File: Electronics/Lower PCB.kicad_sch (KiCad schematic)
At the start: 30 parts, among them J6 Conn_01x04_Male, SW1 Left, SW2 Right, U1 QRE1113GR, U13 TCST2103, TCST2202, TCST2300, U14 TCST2103, TCST2202, TCST2300, U2 QRE1113GR, U3 QRE1113GR, U4 QRE1113GR, U5 QRE1113GR

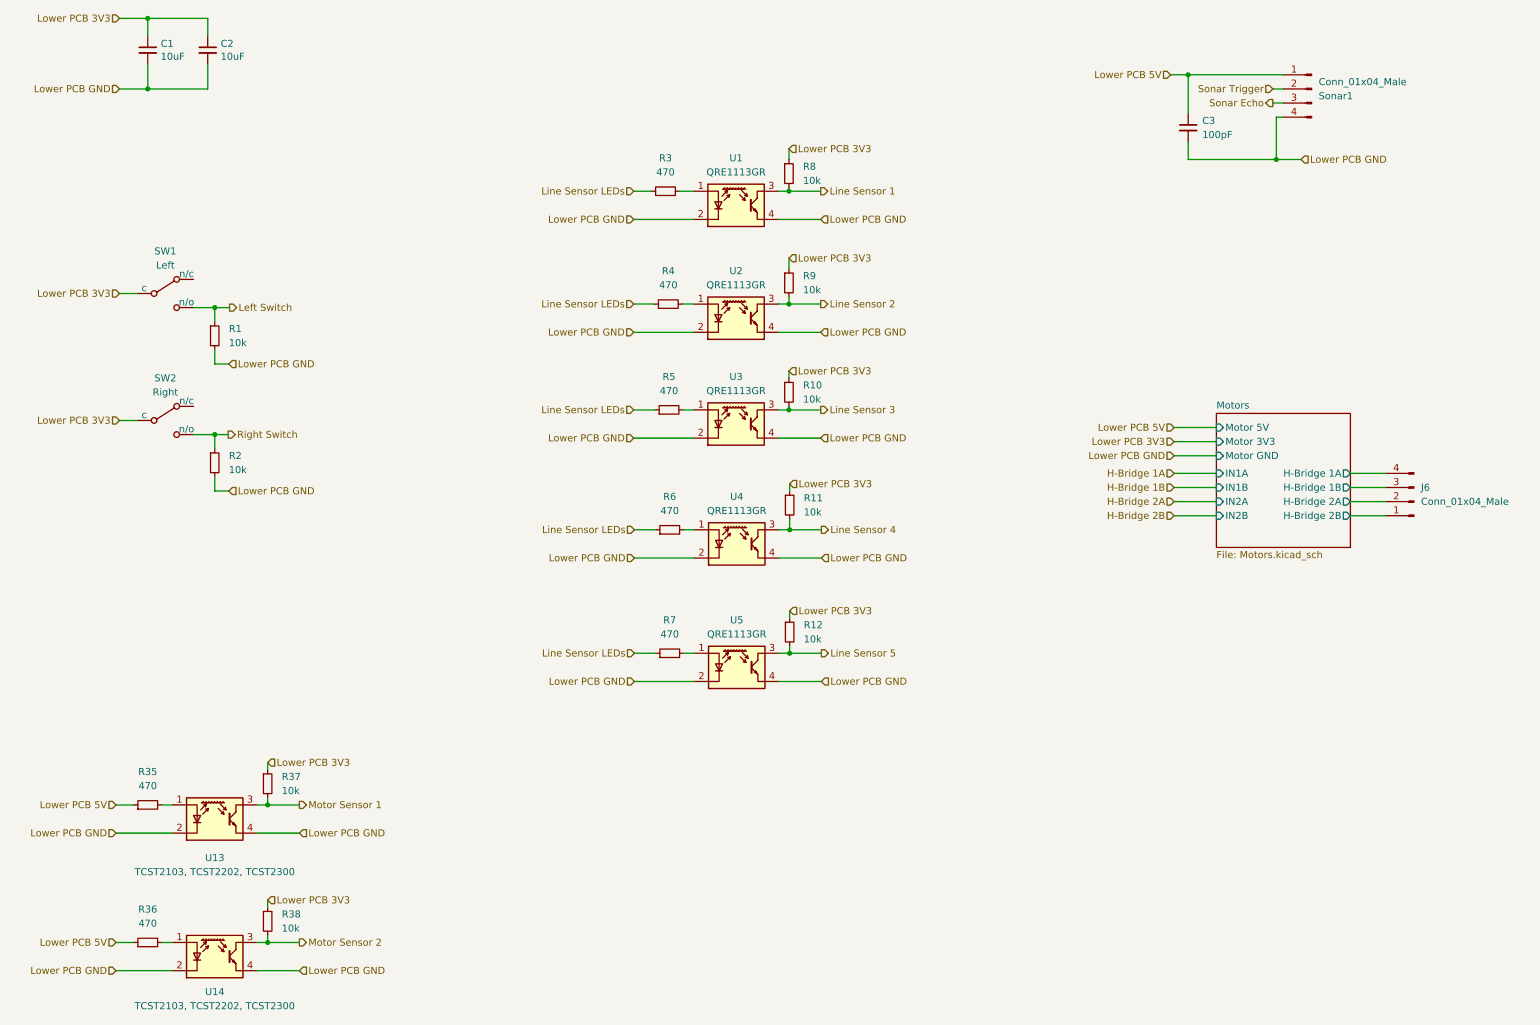
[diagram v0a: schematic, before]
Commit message: added bom
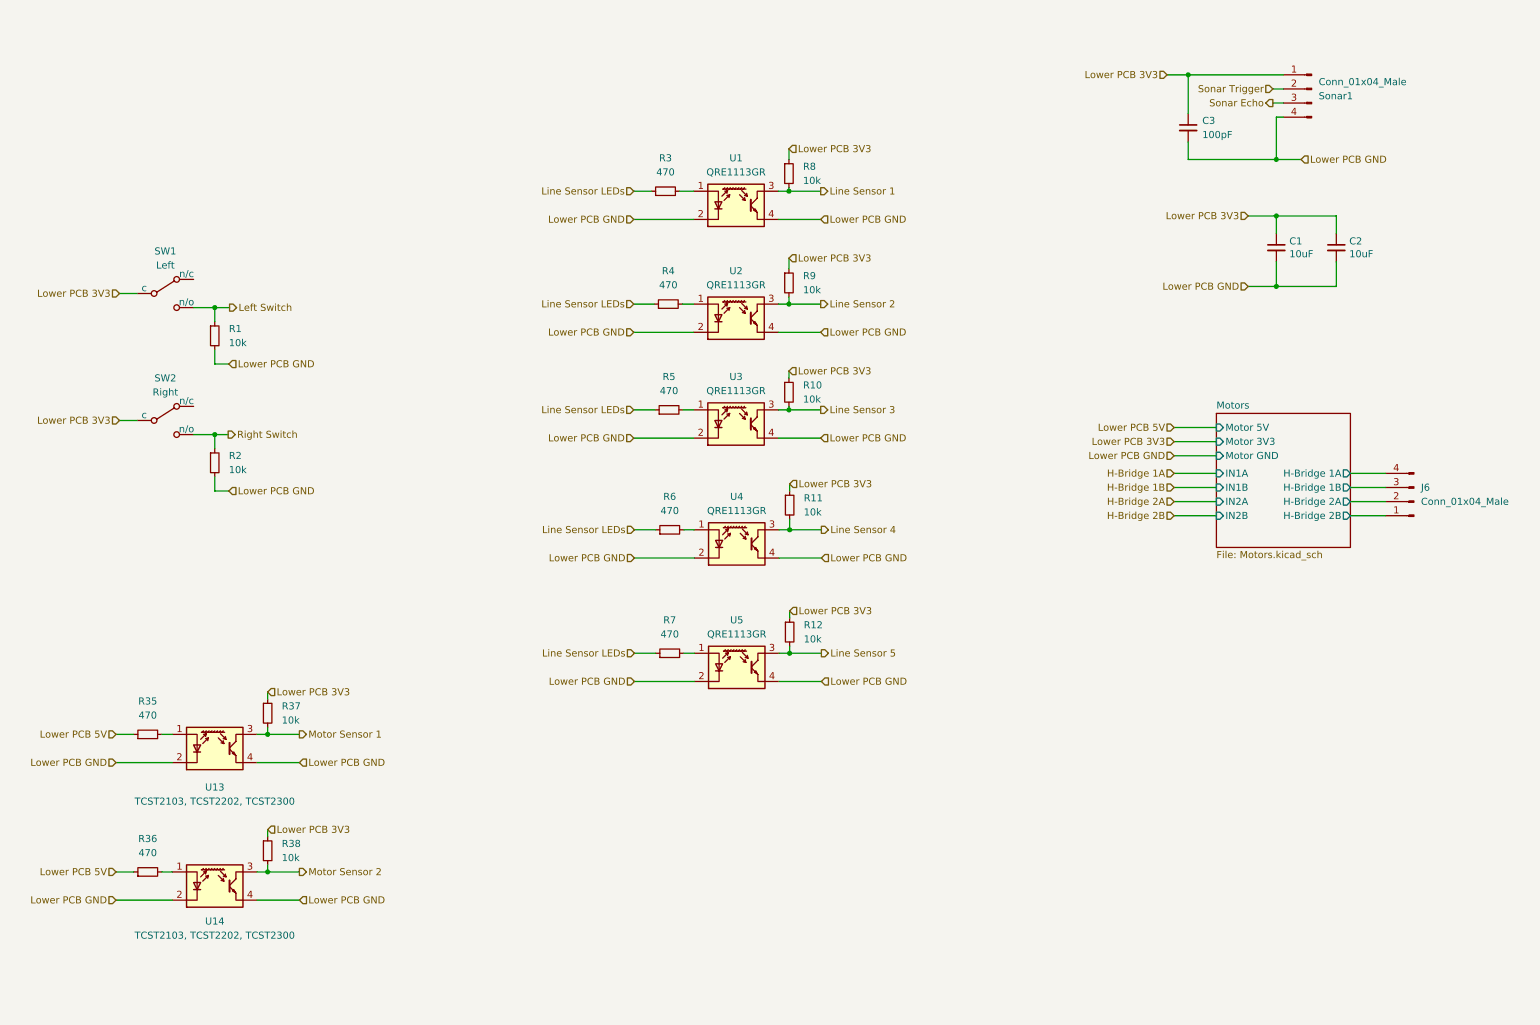
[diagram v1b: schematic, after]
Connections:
- net Lower PCB 3V3: now also C3.1, Sonar1.1 (Pin_1)
- net Lower PCB 5V: no longer C3.1, Sonar1.1 (Pin_1)
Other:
- moved on the sheet: C1, C2, R35, R36, R37, R38, U13, U14

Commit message: del backups
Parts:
- renumbered C3 to C7, C1 to C8, C2 to C9, J6 to J4, R35 to R1, R6 to R10, R7 to R11, R8 to R12, R9 to R13, R10 to R14, R11 to R15, R12 to R16, R36 to R2, R1 to R3, R2 to R4, R37 to R5, R38 to R6, R3 to R7, R4 to R8, R5 to R9, U13 to U2, U14 to U3, U1 to U4, U2 to U5, U3 to U6, U4 to U7, U5 to U8
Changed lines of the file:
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@@
   (symbol (lib_id "Device:R_Small") (at 43.815 149.225 90) (unit 1)
     (in_bom yes) (on_board yes) (fields_autoplaced)
-    (property "Reference" "R35" (id 0) (at 43.815 143.256 90))
+    (property "Reference" "R1" (id 0) (at 43.815 143.256 90))
     (property "Value" "470" (id 1) (at 43.815 145.796 90))
     (property "Footprint" "Resistor_SMD:R_0805_2012Metric_Pad1.20x1.40mm_HandSolder" (id 2) (at 43.815 149.225 0)
@@
   (symbol (lib_id "Device:R_Small") (at 43.815 173.99 90) (unit 1)
     (in_bom yes) (on_board yes) (fields_autoplaced)
-    (property "Reference" "R36" (id 0) (at 43.815 168.021 90))
+    (property "Reference" "R2" (id 0) (at 43.815 168.021 90))
     (property "Value" "470" (id 1) (at 43.815 170.561 90))
     (property "Footprint" "Resistor_SMD:R_0805_2012Metric_Pad1.20x1.40mm_HandSolder" (id 2) (at 43.815 173.99 0)
@@
   (symbol (lib_id "Device:R_Small") (at 55.88 77.47 0) (unit 1)
     (in_bom yes) (on_board yes) (fields_autoplaced)
-    (property "Reference" "R1" (id 0) (at 58.42 76.1999 0)
+    (property "Reference" "R3" (id 0) (at 58.42 76.1999 0)
       (effects (font (size 1.27 1.27)) (justify left))
     )
@@
   (symbol (lib_id "Device:R_Small") (at 55.88 100.33 0) (unit 1)
     (in_bom yes) (on_board yes) (fields_autoplaced)
-    (property "Reference" "R2" (id 0) (at 58.42 99.0599 0)
+    (property "Reference" "R4" (id 0) (at 58.42 99.0599 0)
       (effects (font (size 1.27 1.27)) (justify left))
     )
@@
   (symbol (lib_id "Device:R_Small") (at 65.405 145.415 0) (unit 1)
     (in_bom yes) (on_board yes) (fields_autoplaced)
-    (property "Reference" "R37" (id 0) (at 67.945 144.1449 0)
+    (property "Reference" "R5" (id 0) (at 67.945 144.1449 0)
       (effects (font (size 1.27 1.27)) (justify left))
     )
@@
   (symbol (lib_id "Device:R_Small") (at 65.405 170.18 0) (unit 1)
     (in_bom yes) (on_board yes) (fields_autoplaced)
-    (property "Reference" "R38" (id 0) (at 67.945 168.9099 0)
+    (property "Reference" "R6" (id 0) (at 67.945 168.9099 0)
       (effects (font (size 1.27 1.27)) (justify left))
     )
@@
   (symbol (lib_id "Device:R_Small") (at 137.033 51.435 90) (unit 1)
     (in_bom yes) (on_board yes) (fields_autoplaced)
-    (property "Reference" "R3" (id 0) (at 137.033 45.466 90))
+    (property "Reference" "R7" (id 0) (at 137.033 45.466 90))
     (property "Value" "470" (id 1) (at 137.033 48.006 90))
     (property "Footprint" "Resistor_SMD:R_0805_2012Metric_Pad1.20x1.40mm_HandSolder" (id 2) (at 137.033 51.435 0)
@@
   (symbol (lib_id "Device:R_Small") (at 137.541 71.755 90) (unit 1)
     (in_bom yes) (on_board yes) (fields_autoplaced)
-    (property "Reference" "R4" (id 0) (at 137.541 65.786 90))
+    (property "Reference" "R8" (id 0) (at 137.541 65.786 90))
     (property "Value" "470" (id 1) (at 137.541 68.326 90))
     (property "Footprint" "Resistor_SMD:R_0805_2012Metric_Pad1.20x1.40mm_HandSolder" (id 2) (at 137.541 71.755 0)
@@
   (symbol (lib_id "Device:R_Small") (at 137.668 90.805 90) (unit 1)
     (in_bom yes) (on_board yes) (fields_autoplaced)
-    (property "Reference" "R5" (id 0) (at 137.668 84.836 90))
+    (property "Reference" "R9" (id 0) (at 137.668 84.836 90))
     (property "Value" "470" (id 1) (at 137.668 87.376 90))
     (property "Footprint" "Resistor_SMD:R_0805_2012Metric_Pad1.20x1.40mm_HandSolder" (id 2) (at 137.668 90.805 0)
@@
   (symbol (lib_id "Device:R_Small") (at 137.795 112.395 90) (unit 1)
     (in_bom yes) (on_board yes) (fields_autoplaced)
-    (property "Reference" "R6" (id 0) (at 137.795 106.426 90))
+    (property "Reference" "R10" (id 0) (at 137.795 106.426 90))
     (property "Value" "470" (id 1) (at 137.795 108.966 90))
     (property "Footprint" "Resistor_SMD:R_0805_2012Metric_Pad1.20x1.40mm_HandSolder" (id 2) (at 137.795 112.395 0)
@@
   (symbol (lib_id "Device:R_Small") (at 137.795 134.62 90) (unit 1)
     (in_bom yes) (on_board yes) (fields_autoplaced)
-    (property "Reference" "R7" (id 0) (at 137.795 128.651 90))
+    (property "Reference" "R11" (id 0) (at 137.795 128.651 90))
     (property "Value" "470" (id 1) (at 137.795 131.191 90))
     (property "Footprint" "Resistor_SMD:R_0805_2012Metric_Pad1.20x1.40mm_HandSolder" (id 2) (at 137.795 134.62 0)
@@
   (symbol (lib_id "Device:R_Small") (at 159.258 48.26 0) (unit 1)
     (in_bom yes) (on_board yes) (fields_autoplaced)
-    (property "Reference" "R8" (id 0) (at 161.798 46.9899 0)
+    (property "Reference" "R12" (id 0) (at 161.798 46.9899 0)
       (effects (font (size 1.27 1.27)) (justify left))
     )
@@
   (symbol (lib_id "Device:R_Small") (at 159.258 67.945 0) (unit 1)
     (in_bom yes) (on_board yes) (fields_autoplaced)
-    (property "Reference" "R9" (id 0) (at 161.798 66.6749 0)
+    (property "Reference" "R13" (id 0) (at 161.798 66.6749 0)
       (effects (font (size 1.27 1.27)) (justify left))
     )
@@
   (symbol (lib_id "Device:R_Small") (at 159.258 87.63 0) (unit 1)
     (in_bom yes) (on_board yes) (fields_autoplaced)
-    (property "Reference" "R10" (id 0) (at 161.798 86.3599 0)
+    (property "Reference" "R14" (id 0) (at 161.798 86.3599 0)
       (effects (font (size 1.27 1.27)) (justify left))
     )
@@
   (symbol (lib_id "Device:R_Small") (at 159.385 107.95 0) (unit 1)
     (in_bom yes) (on_board yes) (fields_autoplaced)
-    (property "Reference" "R11" (id 0) (at 161.925 106.6799 0)
+    (property "Reference" "R15" (id 0) (at 161.925 106.6799 0)
       (effects (font (size 1.27 1.27)) (justify left))
     )
@@
   (symbol (lib_id "Device:R_Small") (at 159.385 130.81 0) (unit 1)
     (in_bom yes) (on_board yes) (fields_autoplaced)
-    (property "Reference" "R12" (id 0) (at 161.925 129.5399 0)
+    (property "Reference" "R16" (id 0) (at 161.925 129.5399 0)
       (effects (font (size 1.27 1.27)) (justify left))
     )
@@
   (symbol (lib_id "Device:C_Small") (at 231.14 40.005 0) (unit 1)
     (in_bom yes) (on_board yes) (fields_autoplaced)
-    (property "Reference" "C3" (id 0) (at 233.68 38.7349 0)
+    (property "Reference" "C7" (id 0) (at 233.68 38.7349 0)
       (effects (font (size 1.27 1.27)) (justify left))
     )
@@
   (symbol (lib_id "Device:C_Small") (at 247.015 61.595 0) (unit 1)
     (in_bom yes) (on_board yes)
-    (property "Reference" "C1" (id 0) (at 249.3518 60.4266 0)
+    (property "Reference" "C8" (id 0) (at 249.3518 60.4266 0)
       (effects (font (size 1.27 1.27)) (justify left))
     )
@@
   (symbol (lib_id "Device:C_Small") (at 257.81 61.595 0) (unit 1)
     (in_bom yes) (on_board yes)
-    (property "Reference" "C2" (id 0) (at 260.1468 60.4266 0)
+    (property "Reference" "C9" (id 0) (at 260.1468 60.4266 0)
       (effects (font (size 1.27 1.27)) (justify left))
     )
@@
   (symbol (lib_id "Connector:Conn_01x04_Male") (at 271.78 107.315 180) (unit 1)
     (in_bom yes) (on_board yes) (fields_autoplaced)
-    (property "Reference" "J6" (id 0) (at 273.05 104.7749 0)
+    (property "Reference" "J4" (id 0) (at 273.05 104.7749 0)
       (effects (font (size 1.27 1.27)) (justify right))
     )
@@
   (symbol (lib_id "Sensor_Proximity:QRE1113GR") (at 55.88 151.765 0) (unit 1)
     (in_bom yes) (on_board yes) (fields_autoplaced)
-    (property "Reference" "U13" (id 0) (at 55.88 158.75 0))
+    (property "Reference" "U2" (id 0) (at 55.88 158.75 0))
     (property "Value" "TCST2103, TCST2202, TCST2300" (id 1) (at 55.88 161.29 0))
     (property "Footprint" "" (id 2) (at 55.88 156.845 0)
@@
   (symbol (lib_id "Sensor_Proximity:QRE1113GR") (at 55.88 176.53 0) (unit 1)
     (in_bom yes) (on_board yes) (fields_autoplaced)
-    (property "Reference" "U14" (id 0) (at 55.88 182.88 0))
+    (property "Reference" "U3" (id 0) (at 55.88 182.88 0))
     (property "Value" "TCST2103, TCST2202, TCST2300" (id 1) (at 55.88 185.42 0))
     (property "Footprint" "" (id 2) (at 55.88 181.61 0)
@@
   (symbol (lib_id "Sensor_Proximity:QRE1113GR") (at 149.733 53.975 0) (unit 1)
     (in_bom yes) (on_board yes) (fields_autoplaced)
-    (property "Reference" "U1" (id 0) (at 149.733 45.466 0))
+    (property "Reference" "U4" (id 0) (at 149.733 45.466 0))
     (property "Value" "QRE1113GR" (id 1) (at 149.733 48.006 0))
     (property "Footprint" "OptoDevice:OnSemi_CASE100CY" (id 2) (at 149.733 59.055 0)
@@
   (symbol (lib_id "Sensor_Proximity:QRE1113GR") (at 149.733 74.295 0) (unit 1)
     (in_bom yes) (on_board yes) (fields_autoplaced)
-    (property "Reference" "U2" (id 0) (at 149.733 65.786 0))
+    (property "Reference" "U5" (id 0) (at 149.733 65.786 0))
     (property "Value" "QRE1113GR" (id 1) (at 149.733 68.326 0))
     (property "Footprint" "OptoDevice:OnSemi_CASE100CY" (id 2) (at 149.733 79.375 0)
@@
   (symbol (lib_id "Sensor_Proximity:QRE1113GR") (at 149.733 93.345 0) (unit 1)
     (in_bom yes) (on_board yes) (fields_autoplaced)
-    (property "Reference" "U3" (id 0) (at 149.733 84.836 0))
+    (property "Reference" "U6" (id 0) (at 149.733 84.836 0))
     (property "Value" "QRE1113GR" (id 1) (at 149.733 87.376 0))
     (property "Footprint" "OptoDevice:OnSemi_CASE100CY" (id 2) (at 149.733 98.425 0)
@@
   (symbol (lib_id "Sensor_Proximity:QRE1113GR") (at 149.86 114.935 0) (unit 1)
     (in_bom yes) (on_board yes) (fields_autoplaced)
-    (property "Reference" "U4" (id 0) (at 149.86 106.426 0))
+    (property "Reference" "U7" (id 0) (at 149.86 106.426 0))
     (property "Value" "QRE1113GR" (id 1) (at 149.86 108.966 0))
     (property "Footprint" "OptoDevice:OnSemi_CASE100CY" (id 2) (at 149.86 120.015 0)
@@
   (symbol (lib_id "Sensor_Proximity:QRE1113GR") (at 149.86 137.16 0) (unit 1)
     (in_bom yes) (on_board yes) (fields_autoplaced)
-    (property "Reference" "U5" (id 0) (at 149.86 128.651 0))
+    (property "Reference" "U8" (id 0) (at 149.86 128.651 0))
     (property "Value" "QRE1113GR" (id 1) (at 149.86 131.191 0))
     (property "Footprint" "OptoDevice:OnSemi_CASE100CY" (id 2) (at 149.86 142.24 0)

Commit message: some changes were made
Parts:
- added C7: 10uF, Capacitor_SMD:C_0805_2012Metric_Pad1.18x1.45mm_HandSolder, symbol Device:C_Small
- renumbered C9 to C10, C7 to C8, C8 to C9
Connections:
- net Lower PCB 3V3: now also R1.1, R2.1, C7.1
- net Lower PCB 5V: no longer R1.1, R2.1
- net Lower PCB GND: now also C7.2
- net Motors/H-Bridge 1B: now also J4.1 (Pin_1); no longer J4.3 (Pin_3)
- net Motors/H-Bridge 2A: now also J4.3 (Pin_3); no longer J4.2 (Pin_2)
- net Motors/H-Bridge 2B: now also J4.2 (Pin_2); no longer J4.1 (Pin_1)
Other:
- added sheet Bottom PCB Version (Bottom PCB Version.kicad_sch)
- company: (none) -> Squashed Fly
- title: (none) -> Swarmbot

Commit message: removed the backups
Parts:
- renumbered J4 to J5
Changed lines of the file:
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@@
   )
   (junction (at 247.015 55.88) (diameter 0) (color 0 0 0 0))
+  (junction (at 221.615 30.48) (diameter 0) (color 0 0 0 0))
+  (junction (at 231.14 30.48) (diameter 0) (color 0 0 0 0))
+  (junction (at 231.14 45.72) (diameter 0) (color 0 0 0 0))
   (junction (at 159.258 71.755) (diameter 0) (color 0 0 0 0))
   (junction (at 159.385 134.62) (diameter 0) (color 0 0 0 0))
-  (junction (at 221.615 30.48) (diameter 0) (color 0 0 0 0))
+  (junction (at 55.88 95.25) (diameter 0) (color 0 0 0 0))
+  (junction (at 159.258 90.805) (diameter 0) (color 0 0 0 0))
+  (junction (at 247.015 45.72) (diameter 0) (color 0 0 0 0))
+  (junction (at 65.405 173.99) (diameter 0) (color 0 0 0 0))
+  (junction (at 247.015 68.58) (diameter 0) (color 0 0 0 0))
   (junction (at 159.385 112.395) (diameter 0) (color 0 0 0 0))
+  (junction (at 55.88 72.39) (diameter 0) (color 0 0 0 0))
+  (junction (at 65.405 149.225) (diameter 0) (color 0 0 0 0))
   (junction (at 159.258 51.435) (diameter 0) (color 0 0 0 0))
-  (junction (at 231.14 45.72) (diameter 0) (color 0 0 0 0))
-  (junction (at 55.88 95.25) (diameter 0) (color 0 0 0 0))
-  (junction (at 65.405 149.225) (diameter 0) (color 0 0 0 0))
-  (junction (at 159.258 90.805) (diameter 0) (color 0 0 0 0))
-  (junction (at 231.14 30.48) (diameter 0) (color 0 0 0 0))
-  (junction (at 247.015 68.58) (diameter 0) (color 0 0 0 0))
-  (junction (at 55.88 72.39) (diameter 0) (color 0 0 0 0))
-  (junction (at 65.405 173.99) (diameter 0) (color 0 0 0 0))
-  (junction (at 247.015 45.72) (diameter 0) (color 0 0 0 0))
   (wire (pts (xy 247.015 38.1) (xy 247.015 45.72))
     (stroke (width 0) (type default) (color 0 0 0 0))
@@
     (stroke (width 0) (type default) (color 0 0 0 0))
   )
+  (wire (pts (xy 159.258 71.755) (xy 164.973 71.755))
+    (stroke (width 0) (type default) (color 0 0 0 0))
+  )
   (wire (pts (xy 157.353 71.755) (xy 159.258 71.755))
     (stroke (width 0) (type default) (color 0 0 0 0))
   )
-  (wire (pts (xy 159.258 71.755) (xy 164.973 71.755))
-    (stroke (width 0) (type default) (color 0 0 0 0))
-  )
   (wire (pts (xy 63.5 173.99) (xy 65.405 173.99))
     (stroke (width 0) (type default) (color 0 0 0 0))
@@
     (stroke (width 0) (type default) (color 0 0 0 0))
   )
+  (wire (pts (xy 157.353 90.805) (xy 159.258 90.805))
+    (stroke (width 0) (type default) (color 0 0 0 0))
+  )
   (wire (pts (xy 159.258 90.805) (xy 164.973 90.805))
     (stroke (width 0) (type default) (color 0 0 0 0))
   )
-  (wire (pts (xy 157.353 90.805) (xy 159.258 90.805))
-    (stroke (width 0) (type default) (color 0 0 0 0))
-  )
   (wire (pts (xy 157.353 56.515) (xy 164.973 56.515))
     (stroke (width 0) (type default) (color 0 0 0 0))
@@
     (stroke (width 0) (type default) (color 0 0 0 0))
   )
+  (wire (pts (xy 63.5 149.225) (xy 65.405 149.225))
+    (stroke (width 0) (type default) (color 0 0 0 0))
+  )
   (wire (pts (xy 65.405 149.225) (xy 71.12 149.225))
-    (stroke (width 0) (type default) (color 0 0 0 0))
-  )
-  (wire (pts (xy 63.5 149.225) (xy 65.405 149.225))
     (stroke (width 0) (type default) (color 0 0 0 0))
   )
@@
   (symbol (lib_id "Connector:Conn_01x04_Male") (at 271.78 107.315 180) (unit 1)
     (in_bom yes) (on_board yes) (fields_autoplaced)
-    (property "Reference" "J4" (id 0) (at 273.05 104.7749 0)
+    (property "Reference" "J5" (id 0) (at 273.05 104.7749 0)
       (effects (font (size 1.27 1.27)) (justify right))
     )
